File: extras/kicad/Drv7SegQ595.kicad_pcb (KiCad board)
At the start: 2 copper layers, 67.4 x 50.8 mm, 33 parts, among them IC1 74HC595, IC2 74HC595, J1 INTERFACE, J2 PWR_LED_JMP, Q1 MMBT3904, Q2 MMBT3904, Q3 MMBT3904, Q4 MMBT3904

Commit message: Rename all KiCAD files to correspond to this library's name.
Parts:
- DISPLAY1: footprint Drv7Seg2x595:display_7seg_4d_0.56in -> Drv7SegQ595:display_7seg_4d_0.56in
- J1: footprint Drv7Seg2x595:PinHeader_1x05_P2.54mm_Horizontal -> Connector_PinHeader_2.54mm:PinHeader_1x05_P2.54mm_Horizontal
- J2: footprint Drv7Seg2x595:PinHeader_1x02_P2.54mm_Horizontal -> Drv7SegQ595:PinHeader_1x02_P2.54mm_Horizontal
- Q1, Q2, Q3, Q4: footprint Drv7Seg2x595:SOT-23 -> Drv7SegQ595:SOT-23
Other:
- board text added: "Copyright (c) 2025 Dmitriy Efimov aka Erling Sigurdson Licensed under CERN-OHL-P v2 Documentation: github.com/ErlingSigurdson/Drv7SegQ595"
- board text removed: "Copyright (c) 2025 Dmitriy Efimov aka Erling Sigurdson Licensed under CERN-OHL-P v2 Documentation: github.com/ErlingSigurdson/Drv7Seg2x595"
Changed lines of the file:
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@@
 		(property ki_fp_filters "R_*")
 		(sheetname "/")
-		(sheetfile "Drv7Seg2x595.kicad_sch")
+		(sheetfile "Drv7SegQ595.kicad_sch")
 		(attr smd)
 		(fp_line
@@
 		(property ki_fp_filters "C_*")
 		(sheetname "/")
-		(sheetfile "Drv7Seg2x595.kicad_sch")
+		(sheetfile "Drv7SegQ595.kicad_sch")
 		(attr smd)
 		(fp_line
@@
 		(property ki_fp_filters "R_*")
 		(sheetname "/")
-		(sheetfile "Drv7Seg2x595.kicad_sch")
+		(sheetfile "Drv7SegQ595.kicad_sch")
 		(attr smd)
 		(fp_line
@@
 		(property ki_fp_filters "R_*")
 		(sheetname "/")
-		(sheetfile "Drv7Seg2x595.kicad_sch")
+		(sheetfile "Drv7SegQ595.kicad_sch")
 		(attr smd)
 		(fp_line
@@
 		(property ki_fp_filters "DIP*W7.62mm* SOIC*3.9x9.9mm*P1.27mm* TSSOP*4.4x5mm*P0.65mm* SOIC*5.3x10.2mm*P1.27mm* SOIC*7.5x10.3mm*P1.27mm*")
 		(sheetname "/")
-		(sheetfile "Drv7Seg2x595.kicad_sch")
+		(sheetfile "Drv7SegQ595.kicad_sch")
 		(attr through_hole)
 		(fp_line
@@
 		(property ki_fp_filters "R_*")
 		(sheetname "/")
-		(sheetfile "Drv7Seg2x595.kicad_sch")
+		(sheetfile "Drv7SegQ595.kicad_sch")
 		(attr smd)
 		(fp_line
@@
 		(property ki_fp_filters "MountingHole*")
 		(sheetname "/")
-		(sheetfile "Drv7Seg2x595.kicad_sch")
+		(sheetfile "Drv7SegQ595.kicad_sch")
 		(attr exclude_from_pos_files exclude_from_bom)
 		(fp_circle
@@
 		(property ki_fp_filters "R_*")
 		(sheetname "/")
-		(sheetfile "Drv7Seg2x595.kicad_sch")
+		(sheetfile "Drv7SegQ595.kicad_sch")
 		(attr smd)
 		(fp_line
@@
 		)
 	)
-	(footprint "Drv7Seg2x595:PinHeader_1x05_P2.54mm_Horizontal"
+	(footprint "Connector_PinHeader_2.54mm:PinHeader_1x05_P2.54mm_Horizontal"
 		(layer "F.Cu")
 		(at 173.99 87.63)
@@
 		(property "Reference" "J1"
 			(at 4.385 -2.27 0)
-			(layer "F.Fab")
-			(hide yes)
+			(layer "F.SilkS")
 			(effects
 				(font
@@
 		)
 		(property "Value" "INTERFACE"
-			(at 3.908303 -2.772658 0)
-			(layer "F.SilkS")
+			(at 4.385 12.43 0)
+			(layer "F.Fab")
 			(effects
 				(font
@@
 		)
 		(sheetname "/")
-		(sheetfile "Drv7Seg2x595.kicad_sch")
+		(sheetfile "Drv7SegQ595.kicad_sch")
 		(attr through_hole)
 		(fp_line
@@
 			)
 		)
-		(pad "1" thru_hole circle
+		(pad "1" thru_hole rect
 			(at 0 0)
-			(size 1.8 1.8)
+			(size 1.7 1.7)
 			(drill 1)
 			(layers "*.Cu" "*.Mask")
@@
 			(pinfunction "VCC")
 			(pintype "power_out")
-			(thermal_bridge_angle 0)
 		)
 		(pad "2" thru_hole circle
 			(at 0 2.54)
-			(size 1.8 1.8)
+			(size 1.7 1.7)
 			(drill 1)
 			(layers "*.Cu" "*.Mask")
@@
 			(pinfunction "DATA/MOSI")
 			(pintype "output")
-			(thermal_bridge_angle 0)
 		)
 		(pad "3" thru_hole circle
 			(at 0 5.08)
-			(size 1.8 1.8)
+			(size 1.7 1.7)
 			(drill 1)
 			(layers "*.Cu" "*.Mask")
@@
 			(pinfunction "LATCH")
 			(pintype "output")
-			(thermal_bridge_angle 0)
 		)
 		(pad "4" thru_hole circle
 			(at 0 7.62)
-			(size 1.8 1.8)
+			(size 1.7 1.7)
 			(drill 1)
 			(layers "*.Cu" "*.Mask")
@@
 			(pinfunction "SCLK/SCK")
 			(pintype "output")
-			(thermal_bridge_angle 0)
 		)
 		(pad "5" thru_hole circle
 			(at 0 10.16)
-			(size 1.8 1.8)
+			(size 1.7 1.7)
 			(drill 1)
 			(layers "*.Cu" "*.Mask")
@@
 			(pinfunction "GND")
 			(pintype "power_out")
-			(thermal_bridge_angle 0)
 		)
 		(embedded_fonts no)
@@
 		(property ki_fp_filters "R_*")
 		(sheetname "/")
-		(sheetfile "Drv7Seg2x595.kicad_sch")
+		(sheetfile "Drv7SegQ595.kicad_sch")
 		(attr smd)
 		(fp_line
@@
 		(property ki_fp_filters "R_*")
 		(sheetname "/")
-		(sheetfile "Drv7Seg2x595.kicad_sch")
+		(sheetfile "Drv7SegQ595.kicad_sch")
 		(attr smd)
 		(fp_line
@@
 		(property ki_fp_filters "R_*")
 		(sheetname "/")
-		(sheetfile "Drv7Seg2x595.kicad_sch")
+		(sheetfile "Drv7SegQ595.kicad_sch")
 		(attr smd)
 		(fp_line
@@
 		(property ki_fp_filters "R_*")
 		(sheetname "/")
-		(sheetfile "Drv7Seg2x595.kicad_sch")
+		(sheetfile "Drv7SegQ595.kicad_sch")
 		(attr smd)
 		(fp_line
@@
 		(property ki_fp_filters "R_*")
 		(sheetname "/")
-		(sheetfile "Drv7Seg2x595.kicad_sch")
+		(sheetfile "Drv7SegQ595.kicad_sch")
 		(attr smd)
 		(fp_line
@@
 		(property ki_fp_filters "DIP*W7.62mm* SOIC*3.9x9.9mm*P1.27mm* TSSOP*4.4x5mm*P0.65mm* SOIC*5.3x10.2mm*P1.27mm* SOIC*7.5x10.3mm*P1.27mm*")
 		(sheetname "/")
-		(sheetfile "Drv7Seg2x595.kicad_sch")
+		(sheetfile "Drv7SegQ595.kicad_sch")
 		(attr through_hole)
 		(fp_line
@@
 		(property ki_fp_filters "MountingHole*")
 		(sheetname "/")
-		(sheetfile "Drv7Seg2x595.kicad_sch")
+		(sheetfile "Drv7SegQ595.kicad_sch")
 		(attr exclude_from_pos_files exclude_from_bom)
 		(fp_circle
@@
 		(embedded_fonts no)
 	)
-	(footprint "Drv7Seg2x595:display_7seg_4d_0.56in"
+	(footprint "Drv7SegQ595:display_7seg_4d_0.56in"
 		(layer "F.Cu")
 		(at 141.8435 99.314 180)
@@
 		)
 		(sheetname "/")
-		(sheetfile "Drv7Seg2x595.kicad_sch")
+		(sheetfile "Drv7SegQ595.kicad_sch")
 		(attr through_hole)
 		(fp_line
@@
 		)
 	)
-	(footprint "Drv7Seg2x595:SOT-23"
+	(footprint "Drv7SegQ595:SOT-23"
 		(layer "F.Cu")
 		(at 149.63 110.81 180)
@@
 		(property ki_fp_filters "SOT?23*")
 		(sheetname "/")
-		(sheetfile "Drv7Seg2x595.kicad_sch")
+		(sheetfile "Drv7SegQ595.kicad_sch")
 		(attr smd)
 		(fp_line
@@
 		(property ki_fp_filters "R_*")
 		(sheetname "/")
-		(sheetfile "Drv7Seg2x595.kicad_sch")
+		(sheetfile "Drv7SegQ595.kicad_sch")
 		(attr smd)
 		(fp_line
@@
 		(property ki_fp_filters "MountingHole*")
 		(sheetname "/")
-		(sheetfile "Drv7Seg2x595.kicad_sch")
+		(sheetfile "Drv7SegQ595.kicad_sch")
 		(attr exclude_from_pos_files exclude_from_bom)
 		(fp_circle
@@
 		(property ki_fp_filters "R_*")
 		(sheetname "/")
-		(sheetfile "Drv7Seg2x595.kicad_sch")
+		(sheetfile "Drv7SegQ595.kicad_sch")
 		(attr smd)
 		(fp_line
@@
 		(property ki_fp_filters "MountingHole*")
 		(sheetname "/")
-		(sheetfile "Drv7Seg2x595.kicad_sch")
+		(sheetfile "Drv7SegQ595.kicad_sch")
 		(attr exclude_from_pos_files exclude_from_bom)
 		(fp_circle
@@
 		(embedded_fonts no)
 	)
-	(footprint "Drv7Seg2x595:SOT-23"
+	(footprint "Drv7SegQ595:SOT-23"
 		(layer "F.Cu")
 		(at 149.63 95.57 180)
@@
 		(property ki_fp_filters "SOT?23*")
 		(sheetname "/")
-		(sheetfile "Drv7Seg2x595.kicad_sch")
+		(sheetfile "Drv7SegQ595.kicad_sch")
 		(attr smd)
 		(fp_line
@@
 		(property ki_fp_filters "LED* LED_SMD:* LED_THT:*")
 		(sheetname "/")
-		(sheetfile "Drv7Seg2x595.kicad_sch")
+		(sheetfile "Drv7SegQ595.kicad_sch")
 		(attr smd)
 		(fp_line
@@
 		(property ki_fp_filters "C_*")
 		(sheetname "/")
-		(sheetfile "Drv7Seg2x595.kicad_sch")
+		(sheetfile "Drv7SegQ595.kicad_sch")
 		(attr smd)
 		(fp_line
@@
 		(property ki_fp_filters "R_*")
 		(sheetname "/")
-		(sheetfile "Drv7Seg2x595.kicad_sch")
+		(sheetfile "Drv7SegQ595.kicad_sch")
 		(attr smd)
 		(fp_line
@@
 		(property ki_fp_filters "R_*")
 		(sheetname "/")
-		(sheetfile "Drv7Seg2x595.kicad_sch")
+		(sheetfile "Drv7SegQ595.kicad_sch")
 		(attr smd)
 		(fp_line
@@
 		(property ki_fp_filters "R_*")
 		(sheetname "/")
-		(sheetfile "Drv7Seg2x595.kicad_sch")
+		(sheetfile "Drv7SegQ595.kicad_sch")
 		(attr smd)
 		(fp_line
@@
 		)
 	)
-	(footprint "Drv7Seg2x595:SOT-23"
+	(footprint "Drv7SegQ595:SOT-23"
 		(layer "F.Cu")
 		(at 149.63 105.73 180)
@@
 		(property ki_fp_filters "SOT?23*")
 		(sheetname "/")
-		(sheetfile "Drv7Seg2x595.kicad_sch")
+		(sheetfile "Drv7SegQ595.kicad_sch")
 		(attr smd)
 		(fp_line
@@
 		(property ki_fp_filters "R_*")
 		(sheetname "/")
-		(sheetfile "Drv7Seg2x595.kicad_sch")
+		(sheetfile "Drv7SegQ595.kicad_sch")
 		(attr smd)
 		(fp_line
@@
 		)
 	)
-	(footprint "Drv7Seg2x595:SOT-23"
+	(footprint "Drv7SegQ595:SOT-23"
 		(layer "F.Cu")
 		(at 149.63 100.65 180)
@@
 		(property ki_fp_filters "SOT?23*")
 		(sheetname "/")
-		(sheetfile "Drv7Seg2x595.kicad_sch")
+		(sheetfile "Drv7SegQ595.kicad_sch")
 		(attr smd)
 		(fp_line
@@
 		(property ki_fp_filters "R_*")
 		(sheetname "/")
-		(sheetfile "Drv7Seg2x595.kicad_sch")
+		(sheetfile "Drv7SegQ595.kicad_sch")
 		(attr smd)
 		(fp_line
@@
 		)
 	)
-	(footprint "Drv7Seg2x595:PinHeader_1x02_P2.54mm_Horizontal"
+	(footprint "Drv7SegQ595:PinHeader_1x02_P2.54mm_Horizontal"
 		(layer "F.Cu")
 		(at 173.99 102.87)
@@
 		(property "Reference" "J2"
 			(at 4.385 -2.27 0)
-			(layer "F.Fab")
-			(hide yes)
+			(layer "F.SilkS")
 			(effects
 				(font
@@
 		)
 		(property "Value" "PWR_LED_JMP"
-			(at 4.064 -2.286 0)
-			(layer "F.SilkS")
+			(at 4.385 4.81 0)
+			(layer "F.Fab")
 			(effects
 				(font
@@
 		)
 		(sheetname "/")
-		(sheetfile "Drv7Seg2x595.kicad_sch")
+		(sheetfile "Drv7SegQ595.kicad_sch")
 		(attr through_hole)
 		(fp_line
@@
 		)
 	)
-	(gr_text " Copyright (c) 2025 Dmitriy Efimov aka Erling Sigurdson\n           Licensed under CERN-OHL-P v2\nDocumentation: github.com/ErlingSigurdson/Drv7Seg2x595"
+	(gr_text " Copyright (c) 2025 Dmitriy Efimov aka Erling Sigurdson\n           Licensed under CERN-OHL-P v2\nDocumentation: github.com/ErlingSigurdson/Drv7SegQ595"
 		(at 138.9 70.5 90)
 		(layer "B.SilkS")

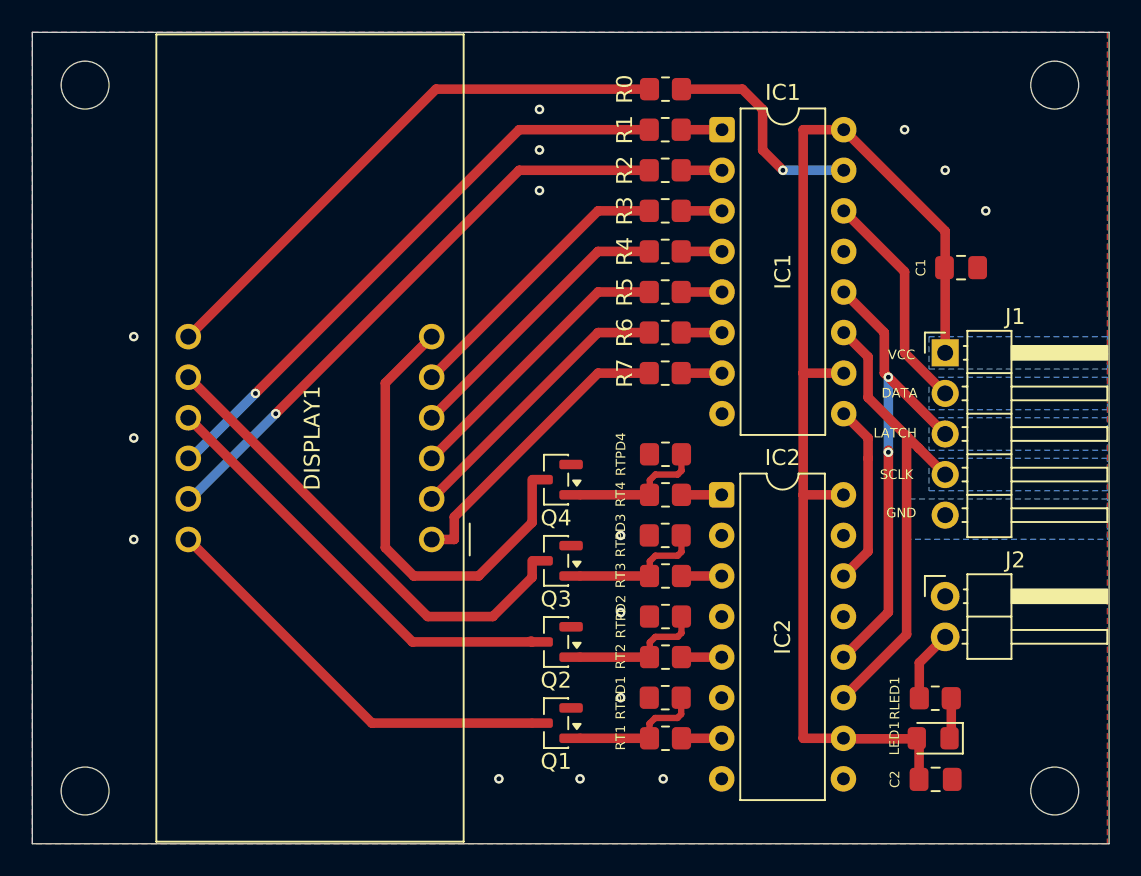
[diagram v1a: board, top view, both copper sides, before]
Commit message: Update KiCAD files contents (mostly schematic) to match this library.
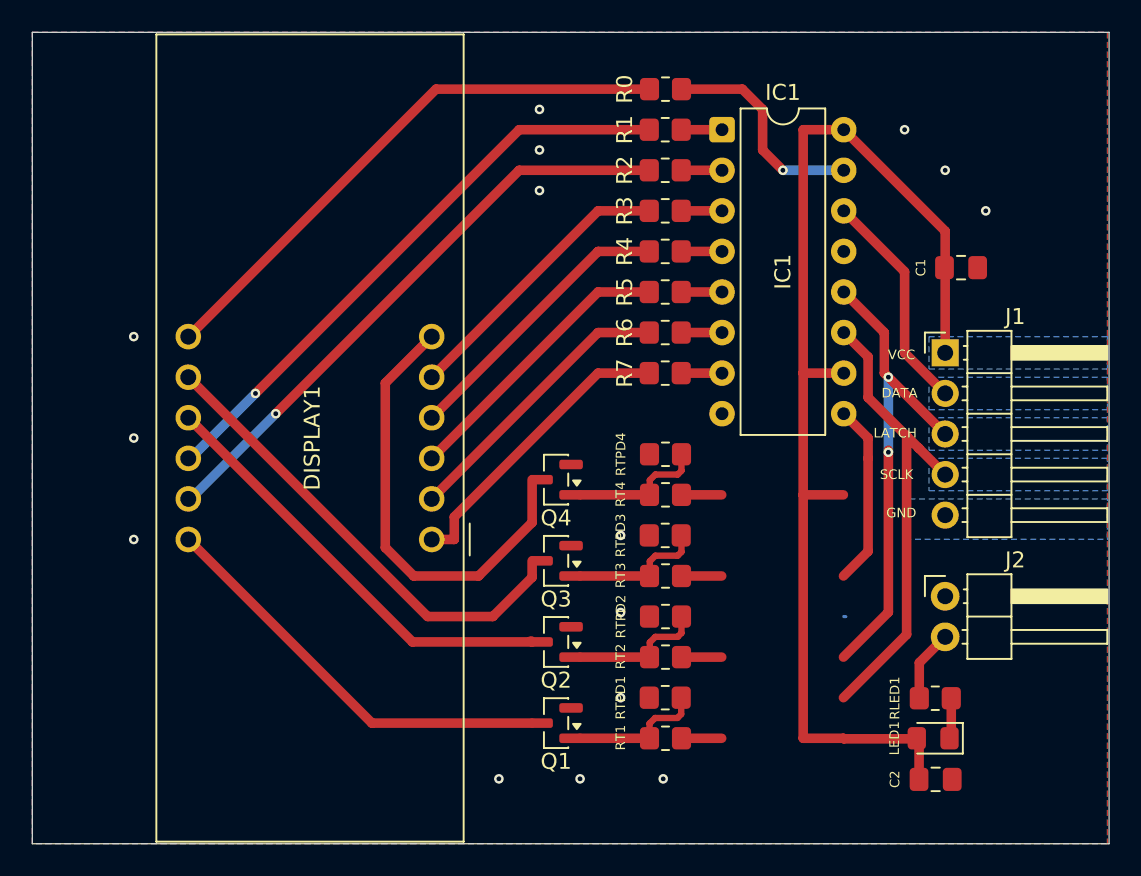
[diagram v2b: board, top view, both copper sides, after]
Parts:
- removed Hole1, Hole2, Hole3, Hole4: MountingHole, MountingHole:MountingHole_3mm
- removed IC2: 74HC595, Package_DIP:DIP-16_W7.62mm
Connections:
- IC1 pad 9: Net-(IC1-Q7S) -> unconnected-(IC1-Q7S-Pad9)
- J1 pad 5: GND -> Net-(J1-D4)
- RT4 pad 2: Net-(IC2-Q1) -> Net-(J1-D4)
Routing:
- net unconnected-(IC1-Q7S-Pad9): track 0.00 -> 11.4 mm
- net Net-(IC1-Q7S): track 11.4 -> 0.00 mm
- net Net-(J1-D4): track 0.00 -> 2.52 mm
- net Net-(IC2-Q1): track 2.52 -> 0.00 mm
